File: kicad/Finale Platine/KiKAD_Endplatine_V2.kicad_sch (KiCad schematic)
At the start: 57 parts, among them J1 Conn_02x08_Odd_Even, J4 Conn_01x03_Pin, Q1 Q_NPN_ECB, Q2 Q_NPN_ECB, Q3 Q_NPN_ECB, Q4 Q_NPN_ECB, U1 NE555P, U2 TL074

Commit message: Platinendesign update mit 2 Induktoren
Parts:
- L1, L2: footprint Inductor_SMD:L_1206_3216Metric_Pad1.42x1.75mm_HandSolder -> TL074:L_Axial_L26.0mm_D14.0mm_P30.48mm_Horizontal_Fastron_JORIS
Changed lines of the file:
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@@
       (effects (font (size 1.27 1.27)) (justify left))
     )
-    (property "Footprint" "Inductor_SMD:L_1206_3216Metric_Pad1.42x1.75mm_HandSolder" (at 116.84 108.712 0)
+    (property "Footprint" "TL074:L_Axial_L26.0mm_D14.0mm_P30.48mm_Horizontal_Fastron_JORIS" (at 116.84 108.712 0)
       (effects (font (size 1.27 1.27)) hide)
     )
@@
       (effects (font (size 1.27 1.27)) (justify left))
     )
-    (property "Footprint" "Inductor_SMD:L_1206_3216Metric_Pad1.42x1.75mm_HandSolder" (at 116.84 99.06 0)
-      (effects (font (size 1.27 1.27)) hide)
-    )
+    (property "Footprint" "TL074:L_Axial_L26.0mm_D14.0mm_P30.48mm_Horizontal_Fastron_JORIS" (at 116.84 99.06 0)
+      (effects (font (size 1.27 1.27)) hide)
+    )

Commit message: Platinenupdate
Platine geupdatet Beschriftung mehr oder weniger gut
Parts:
- added +/L3: 100m, Inductor_THT:L_Radial_D12.0mm_P6.00mm_Murata_1900R, symbol Device:L
- added C6/R1: 1000k, Resistor_SMD:R_1206_3216Metric_Pad1.30x1.75mm_HandSolder, symbol Device:R
- added R12/-1: 100, Resistor_SMD:R_1206_3216Metric_Pad1.30x1.75mm_HandSolder, symbol Device:R
- added RV1/-1: 10k, Connector_JST:JST_EH_S3B-EH_1x03_P2.50mm_Horizontal, symbol Device:R_Potentiometer
- +/L1: renamed from L1; value 560m -> 100m; footprint TL074:L_Axial_L26.0mm_D14.0mm_P30.48mm_Horizontal_Fastron_JORIS -> Inductor_THT:L_Radial_D12.0mm_P6.00mm_Murata_1900R
- +/L2: renamed from L2; value 560m -> 100m; footprint TL074:L_Axial_L26.0mm_D14.0mm_P30.48mm_Horizontal_Fastron_JORIS -> Inductor_THT:L_Radial_D12.0mm_P6.00mm_Murata_1900R
- D2: value D -> C5/D2
- renumbered R21 to +/+1, C14 to +/C14, C15 to +/C15, C6 to +/C6, Q4 to +/Q4, R17 to +/R17, R27 to +/R27, R28 to +/R28, R29 to +/R29, R30 to +/R30, R16 to -/-1, C12 to C1/+1, C1 to C3/C1, C2 to C4/C2, R20 to C6/R3, C11 to C7/+1, C5 to C8/C5, C13 to C9/+1, R2 to D1/R2, Q3 to Q3/+1, R1 to R1/R1, R3 to R10/-1, R19 to R11/+1, R4 to R14/R4, R23 to R16/+1, R26 to R17/+1, R22 to R2/R5, R25 to R3/+1, R24 to R4/+1, D1 to R5/D1, R5 to R6/+1, R15 to R7/-1, R14 to R8/1, C3 to R9/+1
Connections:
- net +12V: now also +/L3.1; no longer +/L2.1
- net GND: now also C6/R1.2, RV1/-1.3; no longer -/-1.2, Q1.1 (E), R9/+1.2
- new net: -/-1.2, C6/R1.1, R9/+1.2
- new net: R12/-1.1, RV1/-1.2
- new net: +/L2.1, +/L3.2
- new net: Q1.1 (E), R12/-1.2
- no-connect marks 10 -> 11
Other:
- moved on the sheet: +/L2

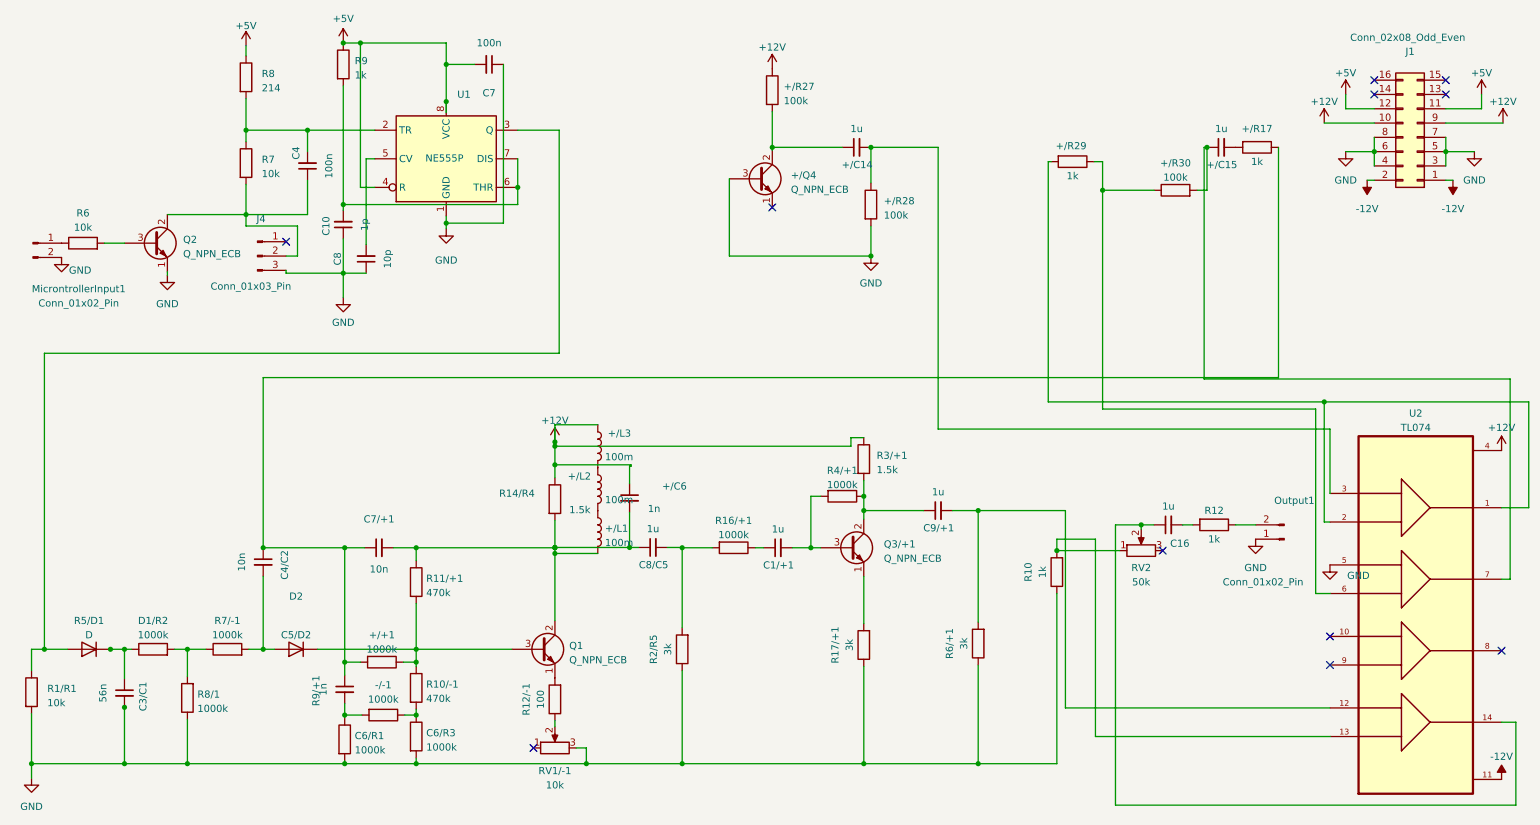
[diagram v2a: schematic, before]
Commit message: Schaltplan verschönert
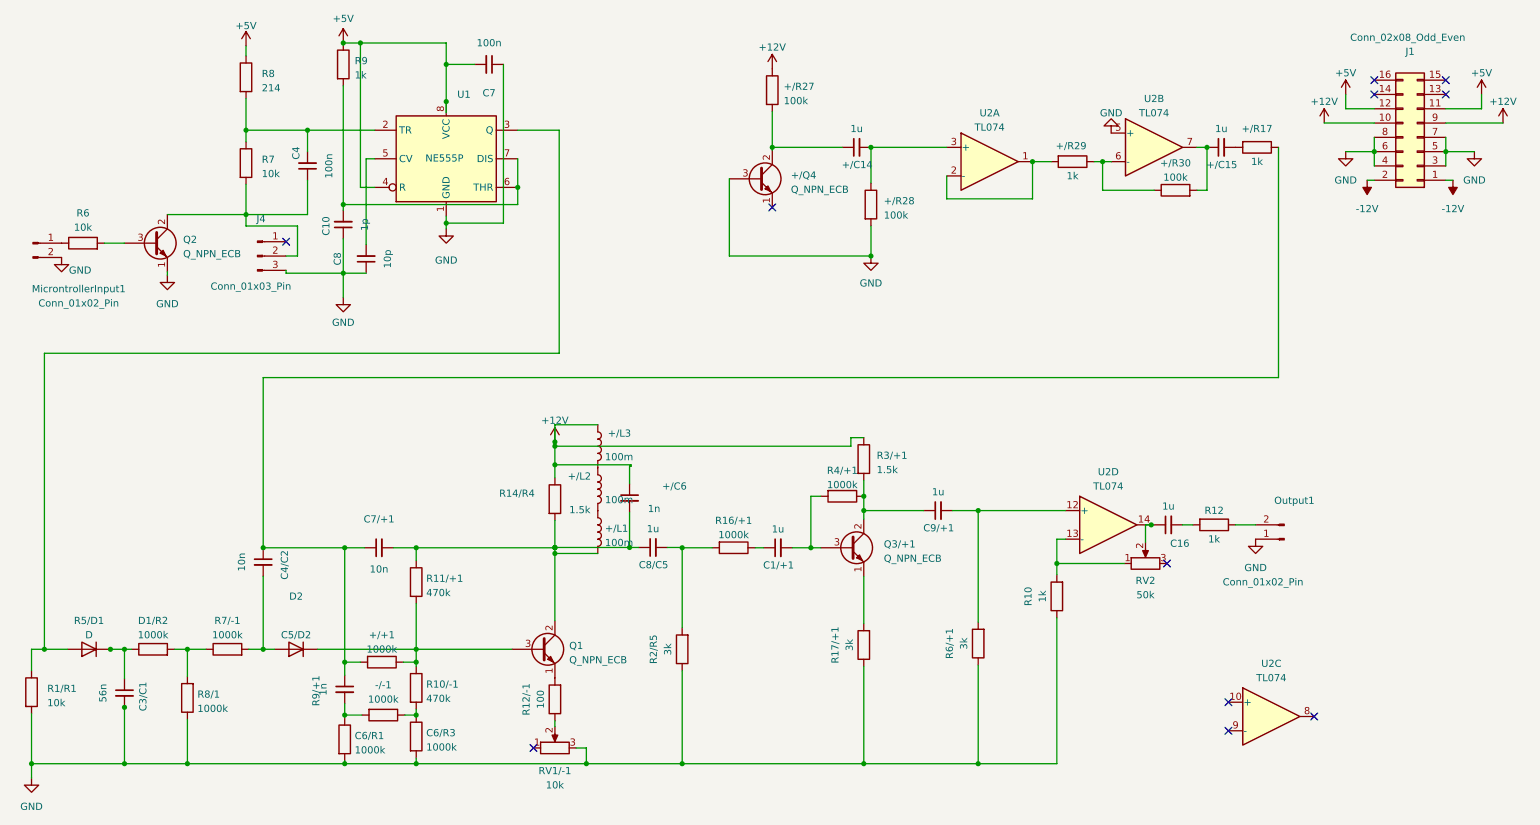
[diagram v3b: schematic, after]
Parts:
- removed U2: TL074, TL074:DIP762W51P254L1994H508Q14, symbol TL074:TL074
- added U2: TL074, Package_DIP:DIP-14_W7.62mm, symbol Amplifier_Operational:TL074
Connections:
- net GND: now also U2.5 (+)
- net at R10.2, RV2.1: now also U2.13 (-)
- net at C16.1, RV2.2: now also U2.14
- net at C9/+1.2, R6/+1.2: now also U2.12 (+)
- net at +/R29.1, +/R30.1: now also U2.6 (-)
- net at +/R29.2: now also U2.1, U2.2 (-)
- net at +/C15.1, +/R30.2: now also U2.7
- net at +/C14.2, +/R28.1: now also U2.3 (+)
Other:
- moved on the sheet: R10, RV2

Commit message: Namenochmal geupdated
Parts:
- renumbered C10 to C21, C4 to C22, C8 to C23, C7 to C24, R6 to R31, R7 to R32, R8 to R33, R9 to R34
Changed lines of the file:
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@@
   (symbol (lib_id "Device:R") (at 25.4 57.404 90) (unit 1)
     (in_bom yes) (on_board yes) (dnp no) (fields_autoplaced)
-    (property "Reference" "R6" (at 25.4 52.07 90)
+    (property "Reference" "R31" (at 25.4 52.07 90)
       (effects (font (size 1.27 1.27)))
     )
@@
       (project "KiKAD_Endplatine_V2"
         (path "/06aebb48-3bd9-4517-ad22-b5366be0f5d8"
-          (reference "R6") (unit 1)
+          (reference "R31") (unit 1)
         )
       )
@@
   (symbol (lib_id "Device:C_Small") (at 65.278 43.688 180) (unit 1)
     (in_bom yes) (on_board yes) (dnp no)
-    (property "Reference" "C4" (at 63.246 41.402 90)
+    (property "Reference" "C22" (at 63.246 41.402 90)
       (effects (font (size 1.27 1.27)))
     )
@@
       (project "KiKAD_Endplatine_V2"
         (path "/06aebb48-3bd9-4517-ad22-b5366be0f5d8"
-          (reference "C4") (unit 1)
+          (reference "C22") (unit 1)
         )
       )
@@
   (symbol (lib_id "Device:R") (at 71.628 25.654 0) (unit 1)
     (in_bom yes) (on_board yes) (dnp no) (fields_autoplaced)
-    (property "Reference" "R9" (at 73.66 25.019 0)
+    (property "Reference" "R34" (at 73.66 25.019 0)
       (effects (font (size 1.27 1.27)) (justify left))
     )
@@
       (project "KiKAD_Endplatine_V2"
         (path "/06aebb48-3bd9-4517-ad22-b5366be0f5d8"
-          (reference "R9") (unit 1)
+          (reference "R34") (unit 1)
         )
       )
@@
   (symbol (lib_id "Device:C_Small") (at 75.692 60.198 180) (unit 1)
     (in_bom yes) (on_board yes) (dnp no)
-    (property "Reference" "C8" (at 70.612 60.1917 90)
+    (property "Reference" "C23" (at 70.612 60.1917 90)
       (effects (font (size 1.27 1.27)))
     )
@@
       (project "KiKAD_Endplatine_V2"
         (path "/06aebb48-3bd9-4517-ad22-b5366be0f5d8"
-          (reference "C8") (unit 1)
+          (reference "C23") (unit 1)
         )
       )
@@
   (symbol (lib_id "Device:R") (at 54.356 43.18 0) (unit 1)
     (in_bom yes) (on_board yes) (dnp no) (fields_autoplaced)
-    (property "Reference" "R7" (at 57.15 42.545 0)
+    (property "Reference" "R32" (at 57.15 42.545 0)
       (effects (font (size 1.27 1.27)) (justify left))
     )
@@
       (project "KiKAD_Endplatine_V2"
         (path "/06aebb48-3bd9-4517-ad22-b5366be0f5d8"
-          (reference "R7") (unit 1)
+          (reference "R32") (unit 1)
         )
       )
@@
   (symbol (lib_id "Device:R") (at 54.356 27.94 0) (unit 1)
     (in_bom yes) (on_board yes) (dnp no) (fields_autoplaced)
-    (property "Reference" "R8" (at 57.15 27.305 0)
+    (property "Reference" "R33" (at 57.15 27.305 0)
       (effects (font (size 1.27 1.27)) (justify left))
     )
@@
       (project "KiKAD_Endplatine_V2"
         (path "/06aebb48-3bd9-4517-ad22-b5366be0f5d8"
-          (reference "R8") (unit 1)
+          (reference "R33") (unit 1)
         )
       )
@@
   (symbol (lib_id "Device:C_Small") (at 71.628 54.102 180) (unit 1)
     (in_bom yes) (on_board yes) (dnp no)
-    (property "Reference" "C10" (at 68.58 54.356 90)
+    (property "Reference" "C21" (at 68.58 54.356 90)
       (effects (font (size 1.27 1.27)))
     )
@@
       (project "KiKAD_Endplatine_V2"
         (path "/06aebb48-3bd9-4517-ad22-b5366be0f5d8"
-          (reference "C10") (unit 1)
+          (reference "C21") (unit 1)
         )
       )
@@
   (symbol (lib_id "Device:C_Small") (at 97.536 25.654 270) (unit 1)
     (in_bom yes) (on_board yes) (dnp no)
-    (property "Reference" "C7" (at 97.5297 30.734 90)
+    (property "Reference" "C24" (at 97.5297 30.734 90)
       (effects (font (size 1.27 1.27)))
     )
@@
       (project "KiKAD_Endplatine_V2"
         (path "/06aebb48-3bd9-4517-ad22-b5366be0f5d8"
-          (reference "C7") (unit 1)
-        )
-      )
+          (reference "C24") (unit 1)
+        )
+      )

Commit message: kicad überarbeitung
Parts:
- added unit 5 of U2
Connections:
- net +12V: now also U2.4 (V+)
- net -12V: now also U2.11 (V-)
- net at C16.1, RV2.2, U2.14: now also RV2.3
- no-connect marks 11 -> 8
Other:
- moved on the sheet: C16, Output1, R12, RV2

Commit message: noch endgültigere finalplatine
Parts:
- added +/R1: 100k, Resistor_SMD:R_1206_3216Metric_Pad1.30x1.75mm_HandSolder, symbol Device:R
- added C1: C, symbol Device:C
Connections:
- net at +/R30.1, U2.6 (-): now also +/R29.2; no longer +/R29.1
- net at U2.1, U2.2 (-): now also U2.10 (+); no longer +/R29.2
- net at U2.8: now also +/R29.1, +/R1.2, C1.2
- net at U2.9 (-): now also +/R1.1, C1.1
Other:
- moved on the sheet: +/C14, +/Q4, +/R27, +/R28, +/R29, U2A, U2C

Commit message: PLATINE endlich fertig glaube ich
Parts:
- added +/RV1, +/RV2, +/RV3, RV/+1, RV/RV/+1: 10k, Connector_JST:JST_EH_S3B-EH_1x03_P2.50mm_Horizontal, symbol Device:R_Potentiometer
- C1: footprint (none) -> Capacitor_SMD:C_1206_3216Metric_Pad1.33x1.80mm_HandSolder
- D2: value C5/D2 -> C5/D2/D2
- MicrontrollerInput1, Output1: footprint Connector_JST:JST_EH_S2B-EH_1x02_P2.50mm_Horizontal -> Connector_JST:JST_EH_S3B-EH_1x03_P2.50mm_Horizontal
- U2: footprint (none) -> Package_DIP:DIP-14_W7.62mm
- renumbered +/C6 to +/C6/C6, R5/D1 to +/D1, +/L2 to +/L2/L2, -/-1 to -/-/-1, C1/+1 to C1/+/-1, C4/C2 to C4/C2/C2, C6/R1 to C6/R1/C3, C7/+1 to C7/+/+1, C8/C5 to C8/C5/C5, C9/+1 to C9/+/-1, D1/R2 to D1/R2/R2, Q3/+1 to Q3/+1/+1, R1/R1 to R1/R1/R1, R11/+1 to R11/+/+1, R14/R4 to R14/R4/R4, R16/+1 to R16/+1/R5, R17/+1 to R17/+/+1, R2/R5 to R2/R5/+1, R3/+1 to R3/+/+1, R4/+1 to R4/+/-1, R6/+1 to R6/+/+1, R7/-1 to R7/-/-1, R8/1 to R8/1/+1, R9/+1 to R9/+/+1, RV1/-1 to RV1k/-/-1
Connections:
- net GND: now also RV1k/-/-1.2, +/RV2.1
- net at C16.1, RV2.2, U2.14: no longer RV2.3
- net at D1/R2/R2.2, R7/-/-1.1: now also RV/RV/+1.2; no longer R8/1/+1.2
- net at -/-/-1.1, C6/R3.1, R10/-1.2: now also +/RV2.2
- net at +/R29.1, C1.2, U2.8: now also +/RV3.2; no longer +/R1.2
- net at +/R29.2, U2.6 (-): now also +/RV1.1; no longer +/R30.1
- net at RV1k/-/-1.1: now also R12/-1.1
- net at +/D1.2 (A), R1/R1/R1.1, U1.3 (Q): now also RV/+1.3
- net at +/D1.1 (K), C3/C1.1, D1/R2/R2.1: now also RV/+1.2
- new net: +/R30.1, +/RV1.2
- new net: +/R1.2, +/RV3.1
- new net: R8/1/+1.2, RV/RV/+1.3
- no-connect marks 8 -> 11
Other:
- moved on the sheet: +/R1, R8/1/+1, RV1k/-/-1

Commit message: alles mögliche
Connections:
- net at +/C14.1, +/R27.2: now also +/Q4.1 (E); no longer +/Q4.2 (C)
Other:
- moved on the sheet: +/C6/C6, +/L1, +/L2/L2, +/L3, C8/C5/C5, R4/+/-1, U2E
